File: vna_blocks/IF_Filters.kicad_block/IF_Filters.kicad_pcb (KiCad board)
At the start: 4 copper layers, 7 parts

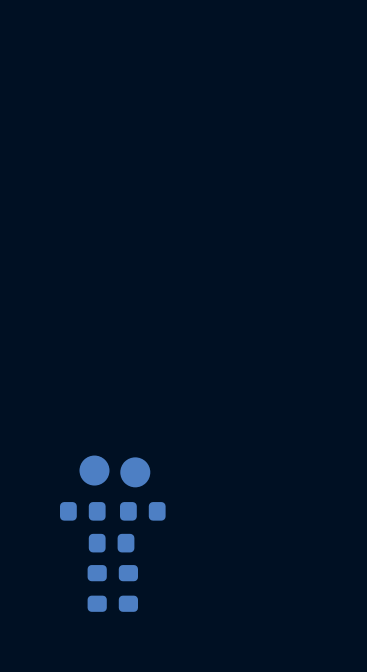
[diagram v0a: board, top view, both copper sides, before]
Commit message: new parts, design blocks updated
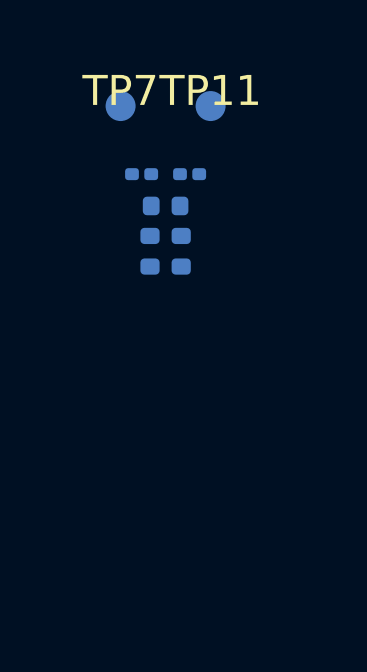
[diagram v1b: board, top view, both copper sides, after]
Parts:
- removed C119, C121: 10p, Capacitor_SMD:C_0402_1005Metric
- removed C120: 27p, Capacitor_SMD:C_0402_1005Metric
- removed R34, R35: 49.9, Resistor_SMD:R_0402_1005Metric
- removed TP4, TP8: IF_TP, VNA_fp:IF_TP
- added C128: 10p, Capacitor_SMD:C_0201_0603Metric, B.Cu at (220.6, 110.5)
- added C129: 27p, Capacitor_SMD:C_0402_1005Metric, B.Cu at (221.4, 111.5)
- added C130: 10p, Capacitor_SMD:C_0201_0603Metric, B.Cu at (222.2, 110.5)
- added R40: 49.9, Resistor_SMD:R_0402_1005Metric, B.Cu at (220.9, 113.0)
- added R41: 49.9, Resistor_SMD:R_0402_1005Metric, B.Cu at (221.9, 113.0)
- added TP11: IF_TP, VNA_fp:IF_TP, F.Cu at (222.9, 108.2)
- added TP7: IF_TP, VNA_fp:IF_TP, F.Cu at (219.9, 108.2)

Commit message: fixed IC courtyard issues
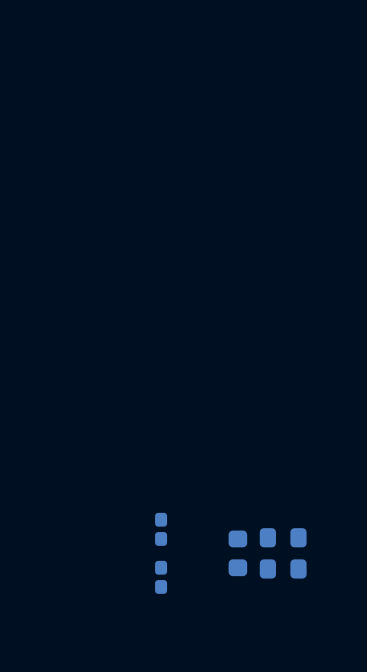
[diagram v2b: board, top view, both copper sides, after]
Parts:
- removed C128, C130: 10p, Capacitor_SMD:C_0201_0603Metric
- removed C129: 27p, Capacitor_SMD:C_0402_1005Metric
- removed R40, R41: 49.9, Resistor_SMD:R_0402_1005Metric
- removed TP11, TP7: IF_TP, VNA_fp:IF_TP
- added C119: 10p, Capacitor_SMD:C_0201_0603Metric, B.Cu at (221.3, 123.9)
- added C120: 27p, Capacitor_SMD:C_0402_1005Metric, B.Cu at (223.8, 123.1)
- added C121: 10p, Capacitor_SMD:C_0201_0603Metric, B.Cu at (221.3, 122.3)
- added R34: 49.9, Resistor_SMD:R_0402_1005Metric, B.Cu at (225.3, 123.6)
- added R35: 49.9, Resistor_SMD:R_0402_1005Metric, B.Cu at (225.3, 122.6)
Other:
- copper layers 4 -> 8
